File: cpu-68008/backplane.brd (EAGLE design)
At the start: 99.7 x 99.7 mm, 24 parts, among them IC1 GAL22V10D, IC2 74HCT245, IC3 74HCT245, IC4 74HCT245, IC5 74HCT245

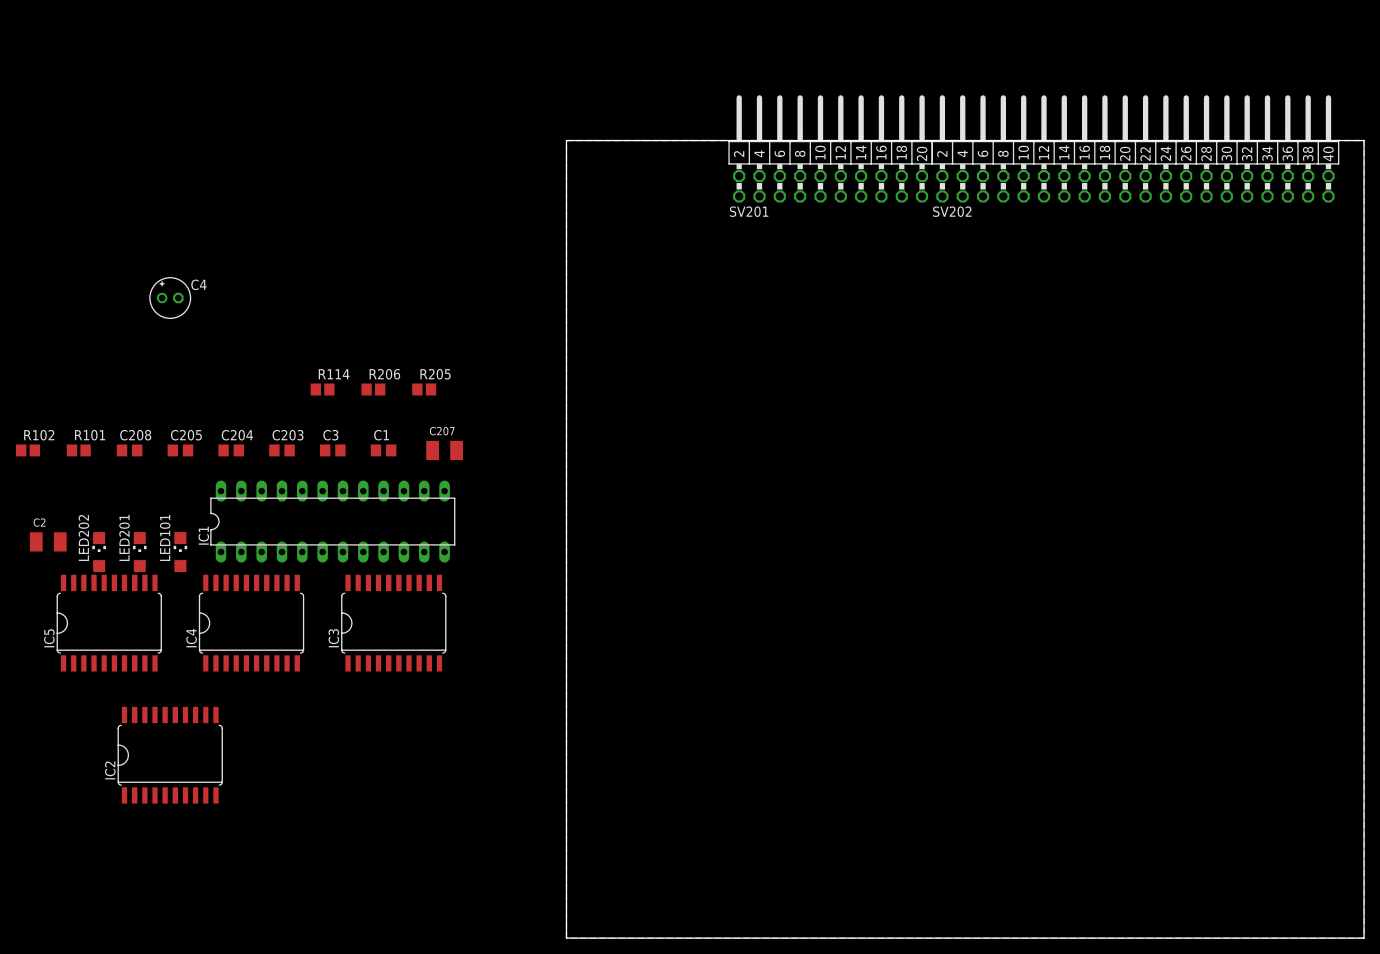
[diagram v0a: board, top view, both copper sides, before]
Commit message: routed level shifters to external connectors
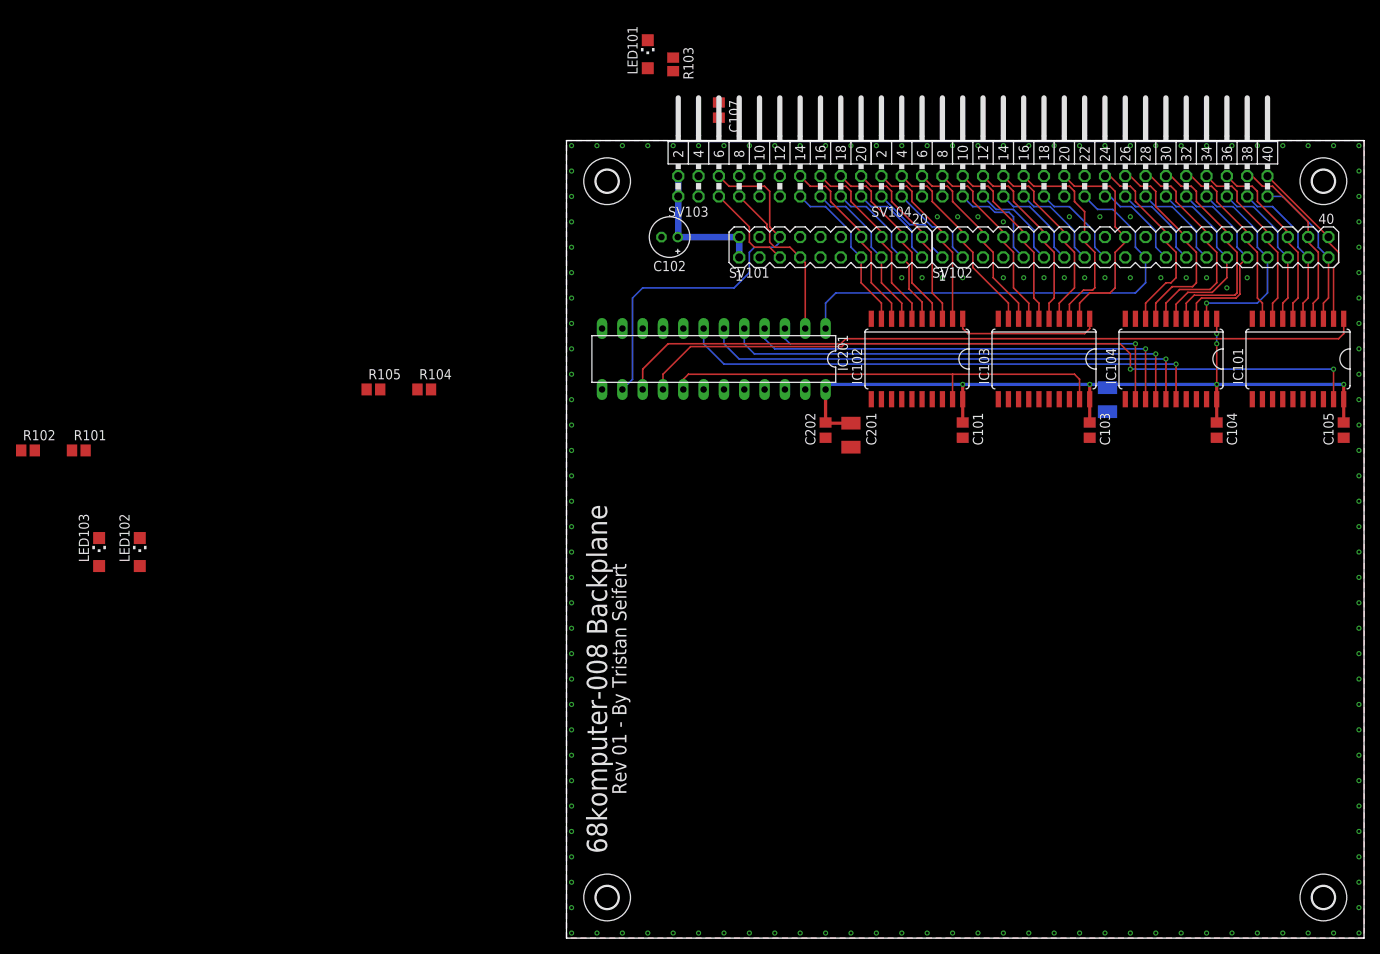
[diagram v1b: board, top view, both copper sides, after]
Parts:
- removed C1, C203, C204, C205, C208, C3: 100nF, rcl:C0805
- removed C2, C207: 10µF, rcl:SMC_B
- removed C4: 47µF, rcl:E2-5
- removed IC1: GAL22V10D, 68komputer:DIL24S
- removed IC2, IC3, IC4, IC5: 74HCT245, 74xx-eu:SO20W
- removed R114: 3k, rcl:R2012
- removed SV201: (no value), con-lstb:MA10-2W
- removed SV202: (no value), con-lstb:MA20-2W
- added C101, C103, C104, C105, C107, C202: 100nF, rcl:C0805
- added C102: 47µF, rcl:E2-5
- added C106, C201: 10µF, rcl:SMC_B
- added H1, H2, H3, H4: MOUNT-HOLE2.8, holes:2,8
- added IC101, IC102, IC103, IC104: 74HCT245, 74xx-eu:SO20W
- added IC201: GAL22V10D, 68komputer:DIL24S
- added R103: 3k, rcl:R2012
- added SV101: (no value), con-lstb:MA10-2
- added SV102: (no value), con-lstb:MA20-2
- added SV103: (no value), con-lstb:MA10-2W
- added SV104: (no value), con-lstb:MA20-2W
- moved LED101 85.4 mm to (10.2, 110.5)
- renumbered LED201 to LED102, LED202 to LED103, R205 to R104, R206 to R105
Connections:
- removed net N$10: IC1.6
- removed net N$11: IC1.7
- net !AS: now also IC104.2, SV102.33, SV104.33; no longer IC5.7, SV202.33
- net !BERR: now also SV102.9, SV104.9; no longer SV202.9
- net !BG: now also SV102.25, SV104.25; no longer SV202.25
- net !BR: now also SV102.23, SV104.23; no longer SV202.23
- net !BUF_ADDR_OE: now also IC102.19, IC103.19, IC201.17; no longer IC1.17, IC3.19, IC4.19
- net !BUF_DATA_OE: now also IC101.19, IC201.16; no longer IC1.15, IC2.19
- net !BUS_CS: now also IC201.2, SV101.7, SV103.7; no longer IC1.2, SV201.7
- net !BUS_DTACK: now also IC201.14, SV101.6, SV103.6; no longer IC1.14, SV201.6
- net !BUS_IRQ: now also SV101.5, SV103.5; no longer SV201.5
- net !DS: now also IC104.3, SV102.31, SV104.31; no longer IC5.8, SV202.31
- net !DTACK: now also SV102.27, SV104.27; no longer SV202.27
- net !HALT: now also SV102.17, SV104.17; no longer SV202.17
- net !RESET: now also SV102.15, SV104.15; no longer SV202.15
- net !SLOT_AS: now also IC104.18; no longer IC5.13
- net !SLOT_CS0: now also IC201.20; no longer IC1.20
- net !SLOT_CS1: now also IC201.21; no longer IC1.21
- net !SLOT_CS2: now also IC201.22; no longer IC1.22
- net !SLOT_CS3: now also IC201.23; no longer IC1.23
- net !SLOT_DS: now also IC104.17; no longer IC5.12
- net !VPA: now also SV102.11, SV104.11; no longer SV202.11
- net +5V: now also C101.1, C102.+, C103.1, C104.1, C105.1, C106.+, C107.1, C201.+, C202.1, IC101.20, IC102.1, IC102.20, IC103.1, IC103.20, IC104.1, IC104.20, IC201.24, R103.1, SV101.1, SV101.2, SV103.1, SV103.2; no longer C1.1, C2.+, C203.1, C204.1, C205.1, C207.+, C208.1, C3.1, C4.+, IC1.24, IC2.20, IC3.1, IC3.20, IC4.1, IC4.20, IC5.1, IC5.20, R114.1, SV201.1, SV201.2
- net A0: now also IC102.5, SV101.17, SV103.17; no longer IC3.2, SV201.17
- net A1: now also IC102.7, SV101.15, SV103.15; no longer IC3.3, SV201.15
- net A10: now also IC103.7, SV102.8, SV104.8; no longer IC4.4, SV202.8
- net A11: now also IC103.6, SV102.10, SV104.10; no longer IC4.5, SV202.10
- net A12: now also IC103.5, SV102.12, SV104.12; no longer IC4.6, SV202.12
- net A13: now also IC103.4, SV102.14, SV104.14; no longer IC4.7, SV202.14
- net A14: now also IC103.3, SV102.16, SV104.16; no longer IC4.8, SV202.16
- net A15: now also IC103.2, SV102.20, SV104.20; no longer IC4.9, SV202.20
- net A16: now also IC104.8, SV102.24, SV104.24; no longer IC5.2, SV202.24
- net A17: now also IC104.7, SV102.26, SV104.26; no longer IC5.3, SV202.26
- net A18: now also IC104.6, SV102.28, SV104.28; no longer IC5.4, SV202.28
- net A19: now also IC104.4, SV102.30, SV104.30; no longer IC5.5, SV202.30
- net A2: now also IC102.9, SV101.13, SV103.13; no longer IC3.4, SV201.13
- net A3: now also IC102.8, SV101.14, SV103.14; no longer IC3.5, SV201.14
- net A4: now also IC102.6, SV101.16, SV103.16; no longer IC3.6, SV201.16
- net A5: now also IC102.4, SV101.18, SV103.18; no longer IC3.7, SV201.18
- net A6: now also IC102.3, SV101.20, SV103.20; no longer IC3.8, SV201.20
- net A7: now also IC102.2, SV102.2, SV104.2; no longer IC3.9, SV202.2
- net A8: now also IC103.9, SV102.4, SV104.4; no longer IC4.2, SV202.4
- net A9: now also IC103.8, SV102.6, SV104.6; no longer IC4.3, SV202.6
- net BUF_DATA_DIR: now also IC101.1, IC201.15; no longer IC1.16, IC2.1
- net CLK: now also IC201.1, SV102.21, SV104.21; no longer IC1.1, SV202.21
- net D0: now also IC101.7, SV102.35, SV104.35; no longer IC2.2, SV202.35
- net D1: now also IC101.5, SV102.37, SV104.37; no longer IC2.3, SV202.37
- net D2: now also IC101.3, SV102.39, SV104.39; no longer IC2.4, SV202.39
- net D3: now also IC101.2, SV102.40, SV104.40; no longer IC2.5, SV202.40
- net D4: now also IC101.4, SV102.38, SV104.38; no longer IC2.6, SV202.38
- net D5: now also IC101.6, SV102.36, SV104.36; no longer IC2.7, SV202.36
- net D6: now also IC101.8, SV102.34, SV104.34; no longer IC2.8, SV202.34
- net D7: now also IC101.9, SV102.32, SV104.32; no longer IC2.9, SV202.32
- net E: now also SV102.13, SV104.13; no longer SV202.13
- net FC0: now also SV101.19, SV103.19; no longer SV201.19
- net FC1: now also SV102.1, SV104.1; no longer SV202.1
- net FC2: now also SV102.3, SV104.3; no longer SV202.3
- net GND: now also C101.2, C102.-, C103.2, C104.2, C105.2, C106.-, C107.2, C201.-, C202.2, IC101.10, IC102.10, IC103.10, IC104.10, IC104.19, IC201.12, SV101.10, SV101.11, SV101.12, SV101.3, SV101.4, SV101.8, SV101.9, SV102.18, SV102.19, SV102.22, SV102.5, SV102.7, SV103.10, SV103.11, SV103.12, SV103.3, SV103.4, SV103.8, SV103.9, SV104.18, SV104.19, SV104.22, SV104.5, SV104.7; no longer C1.2, C2.-, C203.2, C204.2, C205.2, C207.-, C208.2, C3.2, C4.-, IC1.12, IC2.10, IC3.10, IC4.10, IC5.10, IC5.19, SV201.10, SV201.11, SV201.12, SV201.3, SV201.4, SV201.8, SV201.9, SV202.18, SV202.19, SV202.22, SV202.5, SV202.7
- net N$12: now also IC201.8; no longer IC1.8
- net N$13: now also IC201.9; no longer IC1.9
- net N$14: now also IC201.10; no longer IC1.10
- net N$15: now also IC201.11; no longer IC1.11
- net N$16: now also IC201.13; no longer IC1.13
- net N$20: now also IC201.19; no longer IC1.19
- net N$27: now also IC201.18; no longer IC1.18
- net N$4: now also R103.2; no longer R114.2
- net R/!W!: now also IC104.5, SV102.29, SV104.29; no longer IC5.6, SV202.29
- net SLOT_A0: now also IC102.15; no longer IC3.18
- net SLOT_A1: now also IC102.13; no longer IC3.17
- net SLOT_A10: now also IC103.13; no longer IC4.16
- net SLOT_A11: now also IC103.14; no longer IC4.15
- net SLOT_A12: now also IC103.15; no longer IC4.14
- net SLOT_A13: now also IC103.16; no longer IC4.13
- net SLOT_A14: now also IC103.17; no longer IC4.12
- net SLOT_A15: now also IC103.18; no longer IC4.11
- net SLOT_A16: now also IC104.12, IC201.3; no longer IC1.3, IC5.18
- net SLOT_A17: now also IC104.13, IC201.4; no longer IC1.4, IC5.17
- net SLOT_A18: now also IC104.14, IC201.5; no longer IC5.16
- net SLOT_A19: now also IC104.16, IC201.7; no longer IC5.15
- net SLOT_A2: now also IC102.11; no longer IC3.16
- net SLOT_A3: now also IC102.12; no longer IC3.15
- net SLOT_A4: now also IC102.14; no longer IC3.14
- net SLOT_A5: now also IC102.16; no longer IC3.13
- net SLOT_A6: now also IC102.17; no longer IC3.12
- net SLOT_A7: now also IC102.18; no longer IC3.11
- net SLOT_A8: now also IC103.11; no longer IC4.18
- net SLOT_A9: now also IC103.12; no longer IC4.17
- net SLOT_D0: now also IC101.13; no longer IC2.18
- net SLOT_D1: now also IC101.15; no longer IC2.17
- net SLOT_D2: now also IC101.17; no longer IC2.16
- net SLOT_D3: now also IC101.18; no longer IC2.15
- net SLOT_D4: now also IC101.16; no longer IC2.14
- net SLOT_D5: now also IC101.14; no longer IC2.13
- net SLOT_D6: now also IC101.12; no longer IC2.12
- net SLOT_D7: now also IC101.11; no longer IC2.11
- net SLOT_R/!W!: now also IC104.15, IC201.6; no longer IC1.5, IC5.14
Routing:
- net +5V: track 0.00 -> 137.1 mm, vias 0 -> 6
- net BUF_DATA_DIR: track 0.00 -> 93.9 mm
- net !BUF_DATA_OE: track 0.00 -> 93.5 mm, vias 0 -> 2
- net SLOT_A19: track 0.00 -> 66.4 mm, vias 0 -> 1
- net SLOT_R/!W!: track 0.00 -> 63.0 mm, vias 0 -> 1
- net SLOT_A18: track 0.00 -> 59.5 mm, vias 0 -> 1
- net CLK: track 0.00 -> 59.3 mm
- net !BUF_ADDR_OE: track 0.00 -> 56.9 mm
- net SLOT_A17: track 0.00 -> 55.7 mm, vias 0 -> 1
- net SLOT_A16: track 0.00 -> 52.3 mm, vias 0 -> 1
- net !BUS_DTACK: track 0.00 -> 48.8 mm
- net A19: track 0.00 -> 28.2 mm
- net A18: track 0.00 -> 27.5 mm
- net A15: track 0.00 -> 27.4 mm
- net !AS: track 0.00 -> 26.5 mm, vias 0 -> 1
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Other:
- board text added: "68komputer-008 Backplane"
- board text added: "Rev 01 - By Tristan Seifert"

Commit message: finished routing backplane
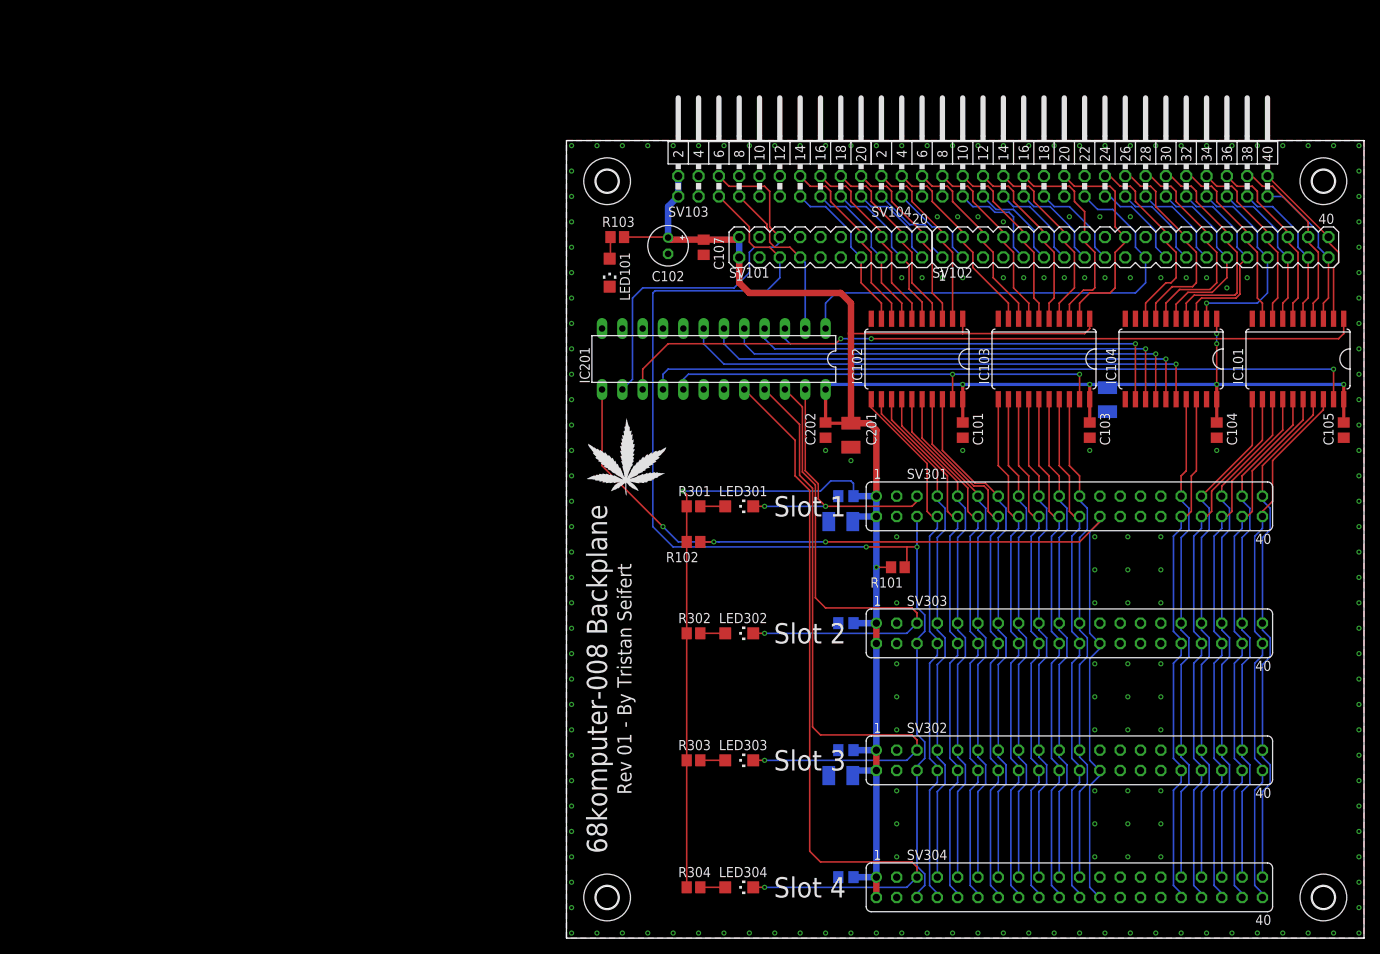
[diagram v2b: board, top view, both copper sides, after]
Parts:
- removed LED102, LED103: (no value), led:CHIPLED_1206
- removed R104, R105: 3k, rcl:R2012
- added C301, C302, C303, C304: 100nF, rcl:C0805
- added C305, C306: 10µF, rcl:SMC_B
- added LED301, LED302, LED303, LED304: (no value), led:CHIPLED_1206
- added R301, R302, R303, R304: 3k, rcl:R2012
- added SV301, SV302, SV303, SV304: (no value), con-lsta:FE20-2
- added WEED301: WEED, 68komputer:DOINK
- moved R101 103.4 mm to (41.4, 46.4), turned to 180 degrees
- moved R102 84.0 mm to (15.9, 49.5), turned to 180 degrees
- moved LED101 27.7 mm to (5.40, 83.2), turned to 180 degrees
- moved R103 22.7 mm to (6.35, 87.6), turned to 180 degrees
- moved C107 17.3 mm to (17.1, 86.4)
- moved C102 1.10 mm to (12.7, 86.6), turned to 270 degrees
- renumbered H1 to H102, H2 to H101, H3 to H103, H4 to H104
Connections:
- removed net !HALT1: R102.1
- removed net N$16: IC201.13
- removed net N$7: LED102.A, R104.2
- removed net N$9: LED103.A, R105.2
- removed net STATUS0: R105.1
- removed net STATUS1: R104.1
- new net !SLOT_ACK: IC201.13, R102.1, SV301.24, SV302.24, SV303.24, SV304.24
- new net N$1: LED302.A, R302.2
- new net N$2: LED301.A, R301.2
- new net N$3: LED304.A, R304.2
- new net N$5: LED303.A, R303.2
- net !BUS_IRQ: now also SV301.6, SV302.6, SV303.6, SV304.6
- net !SLOT_AS: now also SV301.32, SV302.32, SV303.32, SV304.32
- net !SLOT_CS0: now also IC201.23, LED301.C, SV301.5; no longer IC201.20
- net !SLOT_CS1: now also IC201.22, LED302.C, SV303.5; no longer IC201.21
- net !SLOT_CS2: now also IC201.21, LED303.C, SV302.5; no longer IC201.22
- net !SLOT_CS3: now also IC201.20, LED304.C, SV304.5; no longer IC201.23
- net !SLOT_DS: now also SV301.31, SV302.31, SV303.31, SV304.31
- net +5V: now also C301.1, C302.1, C303.1, C304.1, C305.+, C306.+, R301.1, R302.1, R303.1, R304.1, SV301.1, SV301.2, SV302.1, SV302.2, SV303.1, SV303.2, SV304.1, SV304.2
- net GND: now also C301.2, C302.2, C303.2, C304.2, C305.-, C306.-, SV301.25, SV301.26, SV301.27, SV301.28, SV301.3, SV301.4, SV302.25, SV302.26, SV302.27, SV302.28, SV302.3, SV302.4, SV303.25, SV303.26, SV303.27, SV303.28, SV303.3, SV303.4, SV304.25, SV304.26, SV304.27, SV304.28, SV304.3, SV304.4; no longer LED102.C, LED103.C
- net SLOT_A0: now also SV301.12, SV302.12, SV303.12, SV304.12
- net SLOT_A1: now also SV301.10, SV302.10, SV303.10, SV304.10
- net SLOT_A10: now also SV301.18, SV302.18, SV303.18, SV304.18
- net SLOT_A11: now also SV301.17, SV302.17, SV303.17, SV304.17
- net SLOT_A12: now also SV301.20, SV302.20, SV303.20, SV304.20
- net SLOT_A13: now also SV301.19, SV302.19, SV303.19, SV304.19
- net SLOT_A14: now also SV301.22, SV302.22, SV303.22, SV304.22
- net SLOT_A15: now also SV301.21, SV302.21, SV303.21, SV304.21
- net SLOT_A2: now also SV301.8, SV302.8, SV303.8, SV304.8
- net SLOT_A3: now also SV301.7, SV302.7, SV303.7, SV304.7
- net SLOT_A4: now also SV301.9, SV302.9, SV303.9, SV304.9
- net SLOT_A5: now also SV301.11, SV302.11, SV303.11, SV304.11
- net SLOT_A6: now also SV301.14, SV302.14, SV303.14, SV304.14
- net SLOT_A7: now also SV301.13, SV302.13, SV303.13, SV304.13
- net SLOT_A8: now also SV301.16, SV302.16, SV303.16, SV304.16
- net SLOT_A9: now also SV301.15, SV302.15, SV303.15, SV304.15
- net SLOT_D0: now also SV301.35, SV302.35, SV303.35, SV304.35
- net SLOT_D1: now also SV301.37, SV302.37, SV303.37, SV304.37
- net SLOT_D2: now also SV301.39, SV302.39, SV303.39, SV304.39
- net SLOT_D3: now also SV301.40, SV302.40, SV303.40, SV304.40
- net SLOT_D4: now also SV301.38, SV302.38, SV303.38, SV304.38
- net SLOT_D5: now also SV301.36, SV302.36, SV303.36, SV304.36
- net SLOT_D6: now also SV301.34, SV302.34, SV303.34, SV304.34
- net SLOT_D7: now also SV301.33, SV302.33, SV303.33, SV304.33
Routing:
- net +5V: track 137.1 -> 347.4 mm, vias 6 -> 8
- net !BUS_IRQ: track 11.9 -> 147.1 mm, vias 0 -> 2
- net !SLOT_ACK: track 0.00 -> 129.9 mm, vias 0 -> 3
- net !SLOT_CS3: track 0.00 -> 97.6 mm, vias 0 -> 1
- net !SLOT_CS2: track 0.00 -> 80.7 mm, vias 0 -> 1
- net SLOT_A6: track 0.00 -> 69.2 mm
- net SLOT_A1: track 0.00 -> 68.5 mm
- net SLOT_A0: track 0.00 -> 68.5 mm
- net SLOT_A2: track 0.00 -> 68.5 mm
- net SLOT_D5: track 0.00 -> 68.2 mm
- net SLOT_D6: track 0.00 -> 68.2 mm
- net SLOT_D4: track 0.00 -> 68.2 mm
- net SLOT_D3: track 0.00 -> 67.8 mm
- net SLOT_A8: track 0.00 -> 66.1 mm
- net SLOT_A14: track 0.00 -> 66.1 mm
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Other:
- board text added: "Slot 1"
- board text added: "Slot 2"
- board text added: "Slot 3"
- board text added: "Slot 4"
